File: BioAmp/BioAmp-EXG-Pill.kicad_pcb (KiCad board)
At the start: 4 copper layers, 48.2 x 13.2 mm, 44 parts, among them IC3 MAX1169BEUD+, J2 Conn_01x04_Pin, J3 Conn_01x04_Pin, J4 522710469, U1 TL074HIPWR

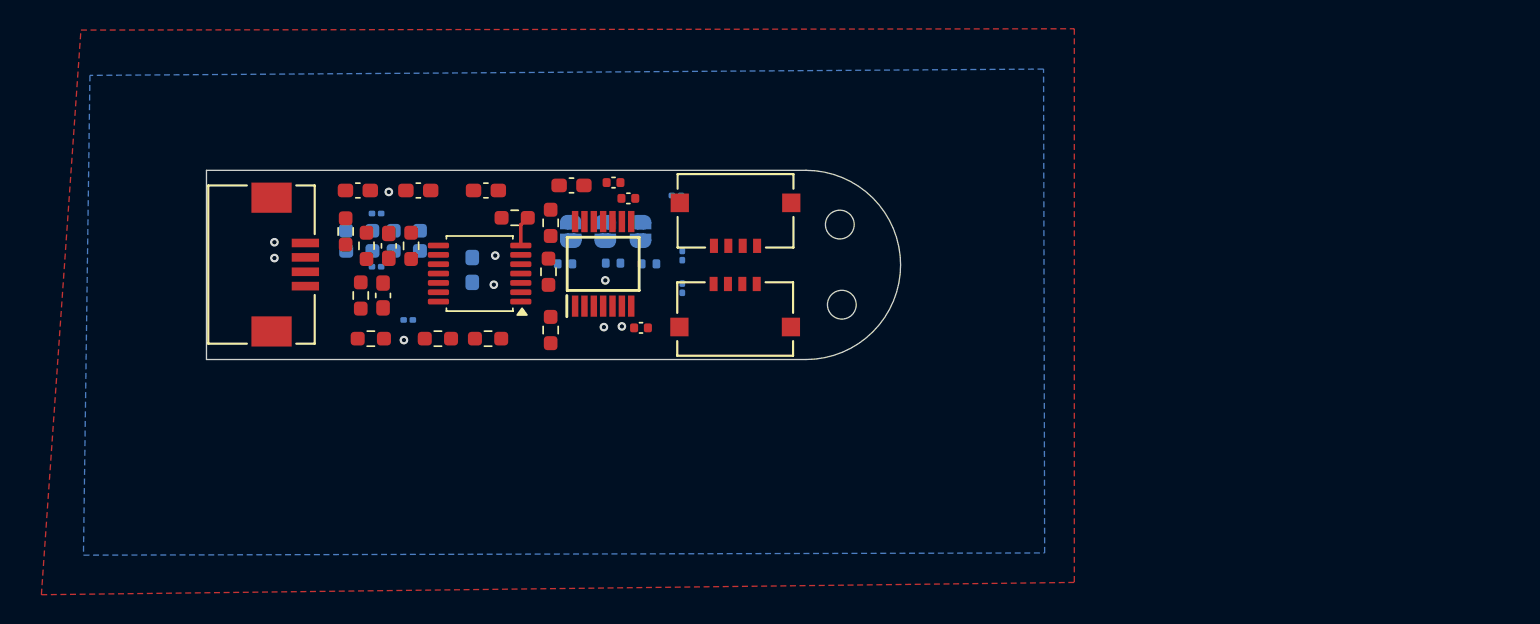
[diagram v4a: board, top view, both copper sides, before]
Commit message: Finished first layout with separated analog and digital grounds
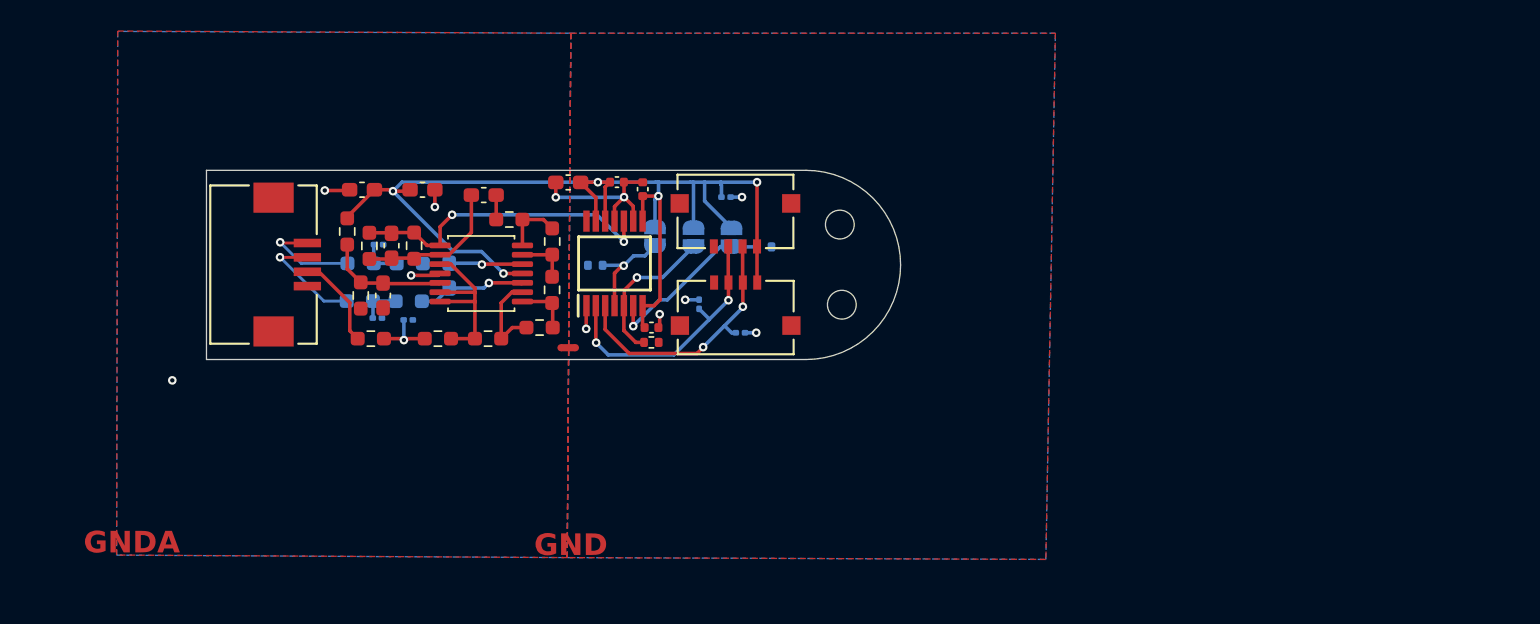
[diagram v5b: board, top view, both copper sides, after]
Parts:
- removed J3: Conn_01x04_Pin, I2C_Connector:CONN_5037630000-SD_04_MOL
- added J1: Conn_01x06_Pin, I2C_Connector:CONN_5037630000-SD_04_MOL, F.Cu at (140.7, 89.9)
- added NT1: NetTie_2, NetTie:NetTie-2_SMD_Pad0.5mm, F.Cu at (129.1, 99.3)
- J2: value Conn_01x04_Pin -> Conn_01x06_Pin
- R18: moved to F.Cu
- moved R19 8.09 mm to (142.7, 92.3)
- moved J2 7.42 mm to (140.8, 97.2), turned to 180 degrees
- moved D1 7.27 mm to (115.9, 97.3)
- moved JP4 6.33 mm to (140.5, 91.7)
- moved JP5 6.14 mm to (137.8, 91.6)
- moved R18 6.12 mm to (134.9, 99.0)
- moved JP6 5.86 mm to (135.2, 91.6)
- moved D5 5.09 mm to (141.1, 98.3), turned to 0 degrees
- moved R6 4.90 mm to (118.0, 96.1)
- moved R13 4.89 mm to (114.6, 96.1)
- moved D6 3.58 mm to (138.2, 96.3)
- moved D4 3.45 mm to (140.1, 88.9)
- moved R17 2.10 mm to (131.0, 93.6)
- moved C4 1.65 mm to (120.8, 94.3)
- moved D2 1.55 mm to (115.9, 92.2)
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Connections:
- C11 pad 1: GND -> GNDA
- C12 pad 1: GND -> GNDA
- C3 pad 2: GND -> GNDA
- C6 pad 1: GND -> GNDA
- C7 pad 1: GND -> GNDA
- C9 pad 1: GND -> GNDA
- D1 pad 2: GND -> GNDA
- D2 pad 2: GND -> GNDA
- D3 pad 2: GND -> GNDA
- IC3 pad 11: GND -> GNDA
- IC3 pad 9: GND -> GNDA
- J2 pad 1: VCC -> GND
- J2 pad 2: SDA -> SCL
- J2 pad 3: SCL -> SDA
- J2 pad 4: GND -> VCC
- J2 pad 5: (no net) -> GND
- J2 pad 6: (no net) -> GND
- J4 pad 1: IN- -> IN+
- J4 pad 2: IN+ -> IN-
- J4 pad 4: unconnected-(J4-Pad4) -> GNDA
- J4 pad P1: unconnected-(J4-PadP1) -> GNDA
- J4 pad P2: unconnected-(J4-PadP2) -> GNDA
- R9 pad 1: GND -> GNDA
- U1 pad 11: GND -> GNDA
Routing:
- net VCC: track 0.00 -> 81.8 mm, vias 1 -> 5
- net bpfOUT: track 0.00 -> 22.2 mm, vias 0 -> 2
- net SDA: track 0.00 -> 18.6 mm, vias 0 -> 2
- net SCL: track 0.00 -> 18.5 mm, vias 0 -> 2
- net GNDA: track 0.00 -> 17.2 mm, vias 0 -> 5
- net ampRef: track 0.00 -> 13.2 mm
- net /ADD0: track 0.00 -> 12.6 mm
- net bpfIN: track 0.00 -> 11.6 mm
- net /ADD1: track 0.00 -> 10.6 mm
- net Net-(U1D-+): track 0.00 -> 8.61 mm
- net IN-: track 0.00 -> 7.80 mm
- net /IN-_Prot: track 0.00 -> 7.78 mm
- net /ADD2: track 0.00 -> 7.53 mm
- net IN+: track 0.00 -> 7.24 mm
- net /IN+_Prot: track 0.00 -> 7.14 mm
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- added copper zone on B.Cu, net GNDA
- added copper zone on F.Cu, net GNDA
- added copper zone on In1.Cu, net GNDA
- added copper zone on In2.Cu, net GNDA
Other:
- board text added: "GNDA"
- board text removed: "SCL"
- board text removed: "SDA"
- board text removed: "VCC"

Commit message: Changed to one mountign hole, improved TVS routing on SCL and SDA
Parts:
- removed the H1 at (148.0, 90.8)
- H1: footprint MountingHole:MountingHole_2mm -> MountingHole:MountingHole_2.5mm_Pad
- moved H1 2.70 mm to (148.7, 93.7)
- moved D6 1.00 mm to (138.1, 97.3), turned to 180 degrees
- moved D5 0.94 mm to (140.4, 97.6), turned to -90 degrees
- moved D1 0.68 mm to (115.2, 97.4), turned to 180 degrees
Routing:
- net GNDA: track 17.2 -> 19.8 mm, vias 5 -> 7
- net SDA: track 18.6 -> 17.7 mm
- net SCL: track 18.5 -> 17.8 mm
- net Net-(D1-K): track 2.78 -> 3.41 mm
- net (no net): vias 1 -> 0
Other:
- board text added: "Analog Ground"
- board text added: "Digital Ground"
- board text removed: "GND"
- board text removed: "GNDA"

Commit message: Moved C6 decoupling capacitor closer to opamp
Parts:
- C6: moved to B.Cu
- moved C6 6.65 mm to (124.6, 91.9), turned to -90 degrees
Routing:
- net VCC: track 81.8 -> 79.3 mm

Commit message: Moved GND/GNDA tie up and placed vias closer to it.
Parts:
- moved NT1 9.79 mm to (129.0, 89.5)
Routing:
- net GND: track 5.31 -> 6.68 mm, vias 5 -> 6
- net GNDA: track 20.1 -> 20.8 mm
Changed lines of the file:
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@@
 	(footprint "NetTie:NetTie-2_SMD_Pad0.5mm"
 		(layer "F.Cu")
-		(at 129.12 99.33 180)
+		(at 128.98 89.54 180)
 		(descr "Net tie, 2 pin, 0.5mm square SMD pads")
 		(tags "net tie")
@@
 	)
 	(segment
+		(start 129.48 89.54)
+		(end 129.48 90.79)
+		(width 0.25)
+		(layer "F.Cu")
+		(net "GND")
+	)
+	(segment
+		(start 129.48 90.79)
+		(end 129.56 90.87)
+		(width 0.25)
+		(layer "F.Cu")
+		(net "GND")
+	)
+	(segment
 		(start 135.48 97)
 		(end 135.48 97.84)
@@
 	)
 	(via
+		(at 129.56 90.87)
+		(size 0.6)
+		(drill 0.3)
+		(layers "F.Cu" "B.Cu")
+		(free yes)
+		(net "GND")
+	)
+	(via
 		(at 135.48 97)
 		(size 0.6)
@@
 	)
 	(segment
+		(start 128.48 89.1)
+		(end 128.2575 88.8775)
+		(width 0.25)
+		(layer "F.Cu")
+		(net "GNDA")
+	)
+	(segment
 		(start 120.065 94.21)
 		(end 120.1 94.175)
@@
 		(width 0.25)
 		(layer "F.Cu")
+		(net "GNDA")
+	)
+	(segment
+		(start 128.48 89.54)
+		(end 128.48 89.1)
+		(width 0.25)
+		(layer "F.Cu")
